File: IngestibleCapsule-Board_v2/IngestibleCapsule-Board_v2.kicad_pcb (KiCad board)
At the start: 2 copper layers, 15 x 55 mm, 52 parts, among them J1 TC2030-NL, J2 AXF6K0412A, J3 AXF5K0412A, J4 513389873, J5 559099872, J6 Conn_01x02_Pin, U1 STM32G473CCUx, U2 MLX90640, U3 ADXL343, U4 W25Q16JVSS, U5 SR1010, Y1 ABM3, Y2 ABS07, Y3 ABS07

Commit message: restarting pcb2
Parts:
- removed C1, C2: 16p, Capacitor_SMD:C_0402_1005Metric
- removed C10, C24: 10u, Capacitor_SMD:C_0603_1608Metric
- removed C11, C12, C13, C14, C17, C21, C5, C6, C7, C8: 100n, Capacitor_SMD:C_0402_1005Metric
- removed C15, C16: 10p, Capacitor_SMD:C_0402_1005Metric
- removed C18, C19, C20, C9: 1u, Capacitor_SMD:C_0402_1005Metric
- removed C22: 680p, Capacitor_SMD:C_0402_1005Metric
- removed C23: 68p, Capacitor_SMD:C_0402_1005Metric
- removed C3, C4: 2p, Capacitor_SMD:C_0402_1005Metric
- removed D1: LED, LED_SMD:LED_0402_1005Metric
- removed J1: TC2030-NL, Connector:Tag-Connect_TC2030-IDC-NL_2x03_P1.27mm_Vertical
- removed J2: AXF6K0412A, kjp_fplib:AXF6K0412A
- removed J3: AXF5K0412A, kjp_fplib:AXF5K0412A
- removed J4: 513389873, kjp_fplib:CON_513389873
- removed J5: 559099872, kjp_fplib:CON_559099872
- removed J6: Conn_01x02_Pin, kjp_fplib:BM02BSRSSTBLFSN
- removed L1: 180n, Inductor_SMD:L_0402_1005Metric
- removed R1, R4: 390R, Resistor_SMD:R_0402_1005Metric
- removed R10, R12: 390k, Resistor_SMD:R_0402_1005Metric
- removed R11: 2M2, Resistor_SMD:R_0603_1608Metric
- removed R2, R5, R6, R7, R8, R9: 10k, Resistor_SMD:R_0402_1005Metric
- removed R3: 0R, Resistor_SMD:R_0402_1005Metric
- removed U1: STM32G473CCUx, Package_DFN_QFN:QFN-48-1EP_7x7mm_P0.5mm_EP5.6x5.6mm
- removed U2: MLX90640, kjp_fplib:MLX90640
- removed U3: ADXL343, Package_LGA:LGA-14_3x5mm_P0.8mm_LayoutBorder1x6y
- removed U4: W25Q16JVSS, Package_SO:SOIC-8_5.3x5.3mm_P1.27mm
- removed U5: SR1010, Package_DFN_QFN:QFN-28-1EP_4x4mm_P0.4mm_EP2.7x2.7mm
- removed Y1: ABM3, kjp_fplib:ABM3-48.000MHZ-B2-T
- removed Y2, Y3: ABS07, kjp_fplib:ABS07-120-32.768KHZ-T
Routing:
- net SPI_GND: track 62.1 -> 0.00 mm, vias 2 -> 0
- net SPI_VDD: track 44.3 -> 0.00 mm, vias 4 -> 0
- net I2C_VDD: track 40.1 -> 0.00 mm
- net I2C_GND: track 35.4 -> 0.00 mm, vias 2 -> 0
- net /SEN_I2C_SDA: track 23.4 -> 0.00 mm
- net /SEN_I2C_SCL: track 21.3 -> 0.00 mm
- net /RF_IRQ: track 13.3 -> 0.00 mm
- net /RF_CS: track 12.7 -> 0.00 mm
- net /MEM_CS: track 12.1 -> 0.00 mm, vias 1 -> 0
- net /SPI_SCK: track 8.83 -> 0.00 mm, vias 2 -> 0
- net /SPI_MOSI: track 8.70 -> 0.00 mm, vias 1 -> 0
- net /SPI_MISO: track 7.97 -> 0.00 mm, vias 1 -> 0
- net Net-(U5-AVDD_1V): track 5.67 -> 0.00 mm
- net Net-(U3-SDO/ADDR): track 5.29 -> 0.00 mm, vias 2 -> 0
- net Net-(U5-XTAL_C2): track 4.99 -> 0.00 mm
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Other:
- board outline removed

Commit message: full v2 implementation, has 5 circles connected by mousebites
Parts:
- added C1: 100n, Capacitor_SMD:C_0402_1005Metric, F.Cu at (85.9, 95.2)
- added C10: 16p, Capacitor_SMD:C_0402_1005Metric, B.Cu at (86.5, 103.4)
- added C11: 2p, Capacitor_SMD:C_0402_1005Metric, B.Cu at (90.0, 94.8)
- added C12: 2p, Capacitor_SMD:C_0402_1005Metric, B.Cu at (90.0, 100.2)
- added C13: 100n, Capacitor_SMD:C_0402_1005Metric, F.Cu at (116.0, 101.8)
- added C14: 100n, Capacitor_SMD:C_0402_1005Metric, F.Cu at (110.0, 106.0)
- added C15: 100n, Capacitor_SMD:C_0402_1005Metric, B.Cu at (95.3, 123.0)
- added C16: 1u, Capacitor_SMD:C_0402_1005Metric, F.Cu at (93.8, 118.0)
- added C17: 1u, Capacitor_SMD:C_0402_1005Metric, F.Cu at (91.9, 114.5)
- added C18: 1u, Capacitor_SMD:C_0402_1005Metric, F.Cu at (93.8, 119.1)
- added C19: 100n, Capacitor_SMD:C_0402_1005Metric, F.Cu at (92.9, 122.2)
- added C2: 100n, Capacitor_SMD:C_0402_1005Metric, B.Cu at (92.1, 96.0)
- added C20: 100n, Capacitor_SMD:C_0402_1005Metric, F.Cu at (93.3, 120.7)
- added C21: 10p, Capacitor_SMD:C_0402_1005Metric, F.Cu at (83.8, 120.8)
- added C22: 10p, Capacitor_SMD:C_0402_1005Metric, F.Cu at (83.8, 118.7)
- added C23: 680p, Capacitor_SMD:C_0402_1005Metric, F.Cu at (85.6, 115.8)
- added C24: 68p, Capacitor_SMD:C_0402_1005Metric, F.Cu at (87.2, 115.3)
- added C3: 100n, Capacitor_SMD:C_0402_1005Metric, F.Cu at (92.8, 96.8)
- added C4: 100n, Capacitor_SMD:C_0402_1005Metric, F.Cu at (91.2, 106.0)
- added C5: 100n, Capacitor_SMD:C_0402_1005Metric, F.Cu at (91.2, 104.8)
- added C6: 1u, Capacitor_SMD:C_0402_1005Metric, F.Cu at (94.7, 103.2)
- added C7: 10u, Capacitor_SMD:C_0603_1608Metric, F.Cu at (93.2, 103.8)
- added C8: 10u, Capacitor_SMD:C_0603_1608Metric, F.Cu at (94.2, 96.2)
- added C9: 16p, Capacitor_SMD:C_0402_1005Metric, B.Cu at (88.0, 94.8)
- added D1: LED, LED_SMD:LED_0402_1005Metric, F.Cu at (89.5, 94.5)
- added J1: DF40C-10DP-0.4V(51), kjp_fplib:DF40C-10DP-0.4V(51), F.Cu at (94.5, 100.0)
- added J2: DF40HB(2.5)-10DS-0.4V(51), kjp_fplib:DF40HB(2.5)-10DS-0.4V(51), B.Cu at (114.5, 100.0)
- added J3: DF40HB(2.5)-10DS-0.4V(51), kjp_fplib:DF40HB(2.5)-10DS-0.4V(51), B.Cu at (90.0, 104.5)
- added J4: DF40C-10DP-0.4V(51), kjp_fplib:DF40C-10DP-0.4V(51), F.Cu at (90.0, 124.5)
- added J5: TC2030-NL, Connector:Tag-Connect_TC2030-IDC-NL_2x03_P1.27mm_Vertical, F.Cu at (90.0, 80.0)
- added J6: Conn_01x02_Pin, kjp_fplib:BM02BSRSSTBLFSN, B.Cu at (90.0, 116.5)
- added J7: HNC2-2.5P-3DS(02), kjp_fplib:HNC2-2.5P-3DS(02), F.Cu at (110.0, 120.0)
- added J8: Conn_01x02_Pin, Connector_PinSocket_2.54mm:PinSocket_1x02_P2.54mm_Vertical, F.Cu at (114.6, 121.1)
- added L1: 180n, Inductor_SMD:L_0402_1005Metric, F.Cu at (91.9, 115.6)
- added R1: 0R, Resistor_SMD:R_0402_1005Metric, B.Cu at (92.1, 94.8)
- added R10: 390k, Resistor_SMD:R_0402_1005Metric, F.Cu at (92.9, 123.4)
- added R11: 2M2, Resistor_SMD:R_0603_1608Metric, F.Cu at (88.5, 114.7)
- added R12: 390k, Resistor_SMD:R_0402_1005Metric, F.Cu at (85.6, 116.9)
- added R2: 10k, Resistor_SMD:R_0402_1005Metric, F.Cu at (87.9, 95.2)
- added R3: 390R, Resistor_SMD:R_0402_1005Metric, B.Cu at (86.5, 102.2)
- added R4: 390R, Resistor_SMD:R_0402_1005Metric, F.Cu at (87.9, 94.1)
- added R5: 10k, Resistor_SMD:R_0402_1005Metric, F.Cu at (112.2, 104.4)
- added R6: 10k, Resistor_SMD:R_0402_1005Metric, F.Cu at (113.5, 104.5)
- added R7: 10k, Resistor_SMD:R_0402_1005Metric, F.Cu at (105.2, 99.0)
- added R8: 10k, Resistor_SMD:R_0402_1005Metric, B.Cu at (84.6, 122.8)
- added R9: 10k, Resistor_SMD:R_0402_1005Metric, F.Cu at (87.6, 122.2)
- added U1: STM32G473CCUx, Package_DFN_QFN:QFN-48-1EP_7x7mm_P0.5mm_EP5.6x5.6mm, F.Cu at (88.0, 100.0)
- added U2: MLX90640, kjp_fplib:MLX90640, F.Cu at (111.0, 101.0)
- added U3: ADXL343, Package_LGA:LGA-14_3x5mm_P0.8mm_LayoutBorder1x6y, F.Cu at (106.5, 103.5)
- added U4: W25Q16JVSS, Package_SO:SOIC-8_5.3x5.3mm_P1.27mm, B.Cu at (90.0, 121.7)
- added U5: SR1010, kjp_fplib:SR1010, F.Cu at (90.0, 119.0)
- added Y1: ABM3, kjp_fplib:ABM3-48.000MHZ-B2-T, B.Cu at (87.2, 98.5)
- added Y2: ABS07, kjp_fplib:ABS07-120-32.768KHZ-T, B.Cu at (90.1, 97.7)
- added Y3: ABS07, kjp_fplib:ABS07-120-32.768KHZ-T, F.Cu at (85.6, 119.8)
- added i2c_2_2: VAL**, v2_mousebites:i2c_2_2, F.Cu at (110.0, 100.0)
- added i2c_2_2: VAL**, v2_mousebites:i2c_2_2, F.Cu at (90.0, 100.0)
- added prog_3_2: VAL**, v2_mousebites:prog_3_2, F.Cu at (90.0, 100.0)
- added prog_3_2: VAL**, v2_mousebites:prog_3_2, F.Cu at (90.0, 80.0)
- added pwr_4_2 (x2): VAL**, v2_mousebites:pwr_4_2, F.Cu at (110.0, 100.0)
- added pwr_4_2: VAL**, v2_mousebites:pwr_4_2, F.Cu at (90.0, 80.0)
- added pwr_4_2: VAL**, v2_mousebites:pwr_4_2, F.Cu at (90.0, 120.0)
- added pwr_4_2 (x2): VAL**, v2_mousebites:pwr_4_2, F.Cu at (110.0, 120.0)
- added spi_4_2: VAL**, v2_mousebites:spi_4_2, F.Cu at (90.0, 100.0)
- added spi_4_2: VAL**, v2_mousebites:spi_4_2, F.Cu at (90.0, 120.0)
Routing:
- net +3.3V: track 0.00 -> 255.6 mm, vias 0 -> 18
- net GND: track 0.00 -> 240.6 mm, vias 0 -> 14
- net /MCU_SPI_MISO: track 0.00 -> 45.2 mm, vias 0 -> 4
- net /MCU_SPI_MOSI: track 0.00 -> 38.2 mm, vias 0 -> 4
- net /MCU_MEM_CS: track 0.00 -> 37.6 mm, vias 0 -> 5
- net /Processor/NRST: track 0.00 -> 37.2 mm, vias 0 -> 2
- net /MCU_I2C_SCL: track 0.00 -> 36.6 mm, vias 0 -> 1
- net /MCU_I2C_SDA: track 0.00 -> 34.2 mm, vias 0 -> 2
- net /MCU_RF_IRQ: track 0.00 -> 31.5 mm, vias 0 -> 5
- net /MCU_SPI_SCK: track 0.00 -> 29.2 mm, vias 0 -> 3
- net /MCU_RF_CS: track 0.00 -> 28.3 mm, vias 0 -> 2
- net /Processor/SWO: track 0.00 -> 17.1 mm
- net /Processor/SWDIO: track 0.00 -> 16.8 mm
- net /Processor/SWCLK: track 0.00 -> 16.2 mm
- net Net-(U1-PF0): track 0.00 -> 10.0 mm, vias 0 -> 1
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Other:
- board outline added: 35 x 55 mm
- board text added: "+3V3"
- board text added: "110,100"
- board text added: "110,120"
- board text added: "90,100"
- board text added: "90,120"
- board text added: "90,80"
- board text added: "GND"
- board text added: "centered at: x=100 y=100"
- board text added: "i2c"
- board text added: "prog"
- board text added: "pwr"
- board text added: "spi"
- board text added: "stm"

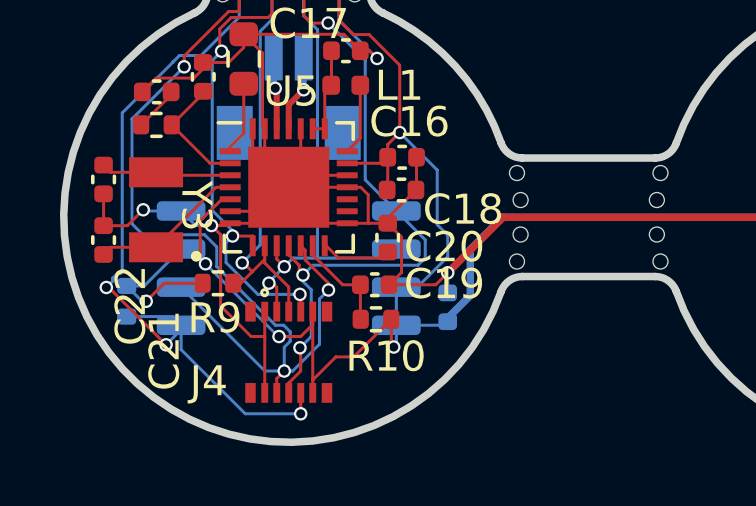
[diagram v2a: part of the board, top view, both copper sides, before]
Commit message: fixed spi connector orientation
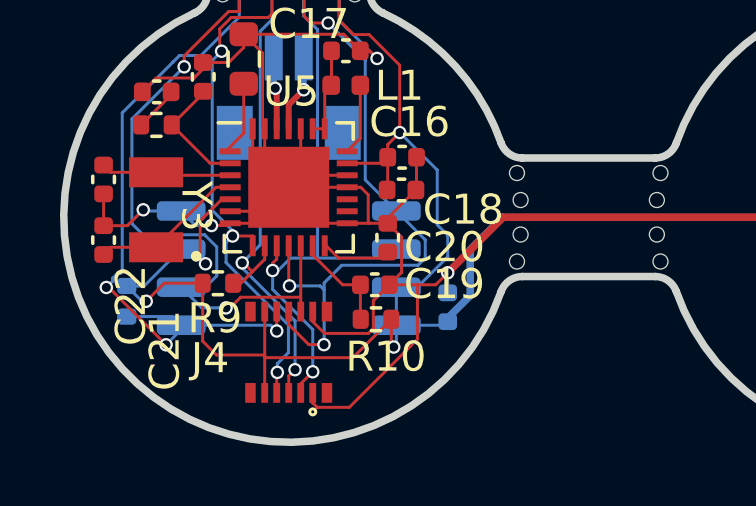
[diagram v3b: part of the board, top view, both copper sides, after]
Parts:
- turned J4 to 180 degrees
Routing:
- net /MCU_SPI_MISO: track 45.2 -> 38.0 mm, vias 4 -> 3
- net GND: track 240.6 -> 244.1 mm
- net /MCU_SPI_SCK: track 29.2 -> 32.6 mm
- net /MCU_RF_CS: track 28.3 -> 31.4 mm, vias 2 -> 3
- net /MCU_MEM_CS: track 37.6 -> 35.1 mm
- net /MCU_RF_IRQ: track 31.5 -> 33.4 mm
- net +3.3V: track 255.6 -> 255.9 mm, vias 18 -> 17
